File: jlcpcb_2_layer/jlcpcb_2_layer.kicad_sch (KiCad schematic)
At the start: 1 part

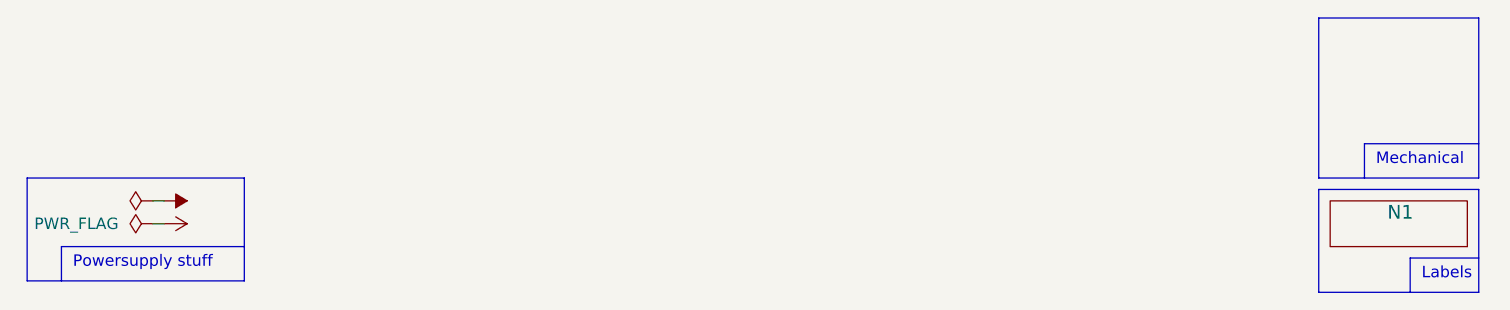
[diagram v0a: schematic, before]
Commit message: updated to kicad V8
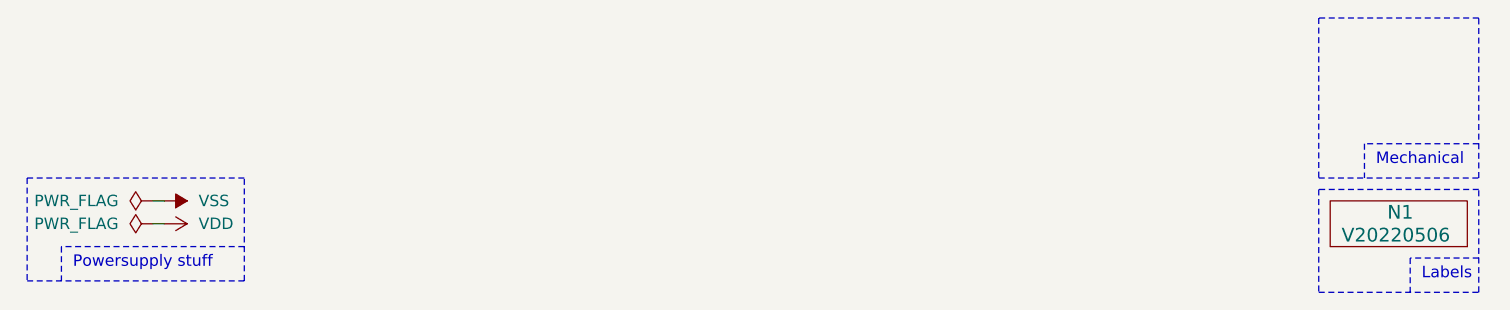
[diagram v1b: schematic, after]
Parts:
- N1: value (none) -> V20220506; footprint (none) -> SquantorLabels:Label_Generic
